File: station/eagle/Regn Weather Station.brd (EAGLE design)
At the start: 66.2 x 49 mm, 6 parts

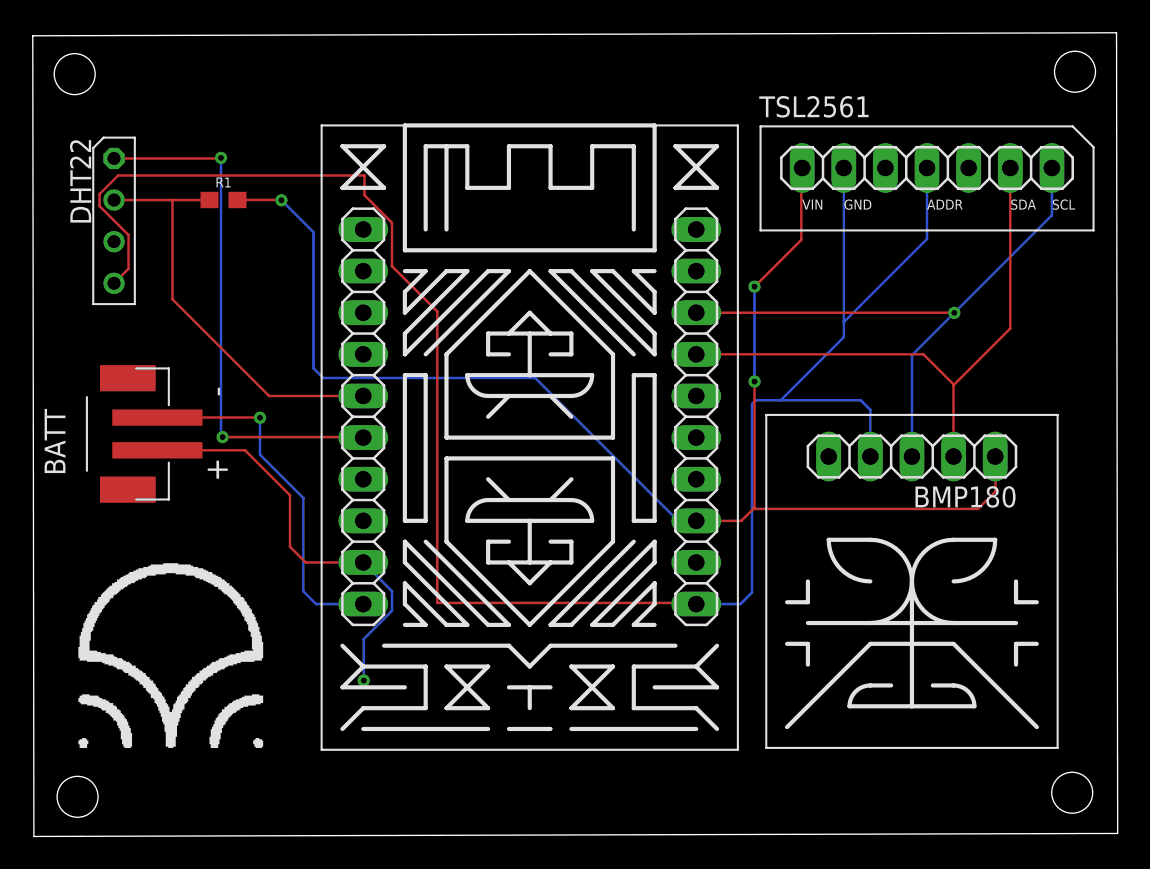
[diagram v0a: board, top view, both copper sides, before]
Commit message: Refactored PCB size and logos
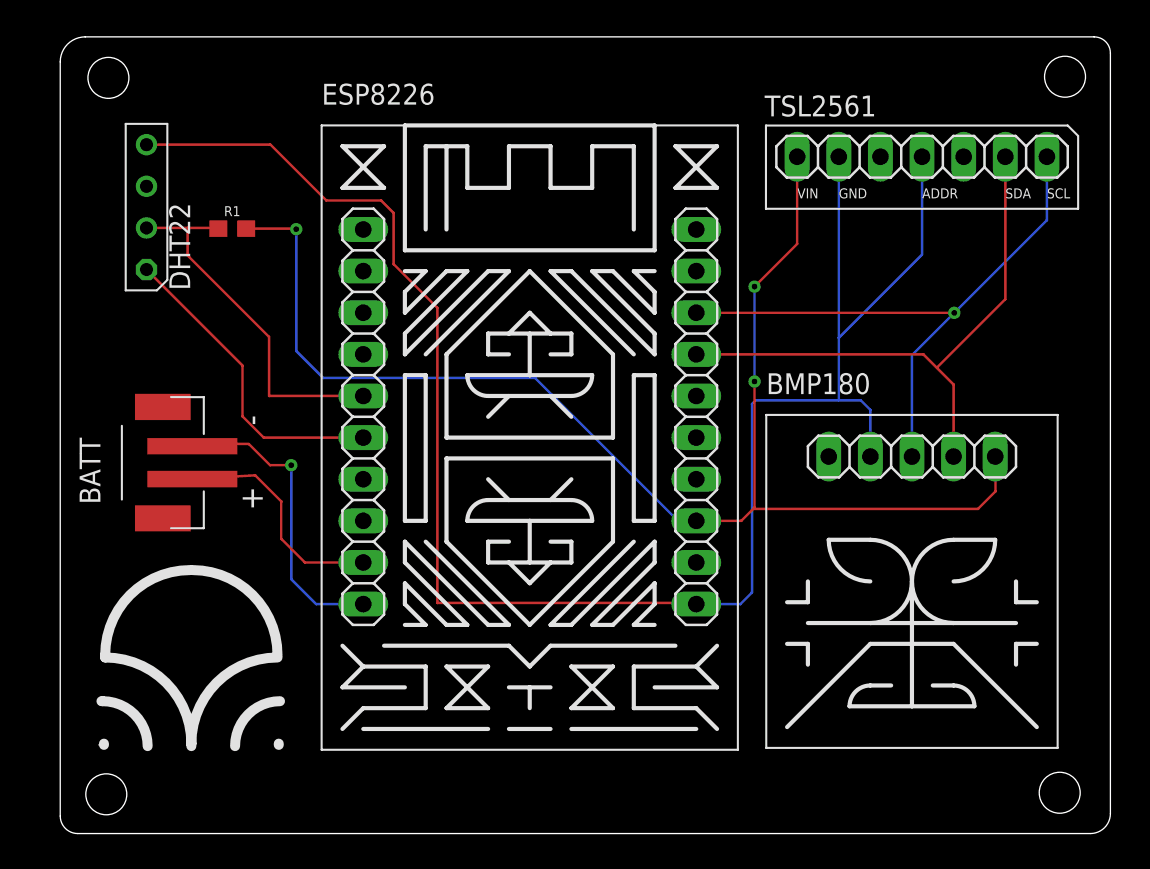
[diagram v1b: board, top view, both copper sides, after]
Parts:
- ESP8226: value ESP8266HUZZAH -> (none)
- moved BATT 2.76 mm to (7.94, 53.9)
- moved DHT22 2.15 mm to (6.94, 69.5), turned to 90 degrees
- moved R1 1.83 mm to (12.2, 68.2)
- moved TSL2561 0.75 mm to (54.3, 72.6)
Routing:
- net N$2: track 32.2 -> 19.3 mm, vias 2 -> 0
- net N$6: track 26.1 -> 14.0 mm, vias 1 -> 0
- net GND: track 120.7 -> 112.8 mm
- net N$1: track 26.0 -> 22.5 mm
- net N$7: track 21.9 -> 18.6 mm
- net 3.3V: track 84.1 -> 82.9 mm
- net N$5: track 36.9 -> 37.5 mm
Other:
- board size 66.2 x 49 mm -> 64.1 x 48.6 mm

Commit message: Increased trace width 0.6 -> 1.0 mil
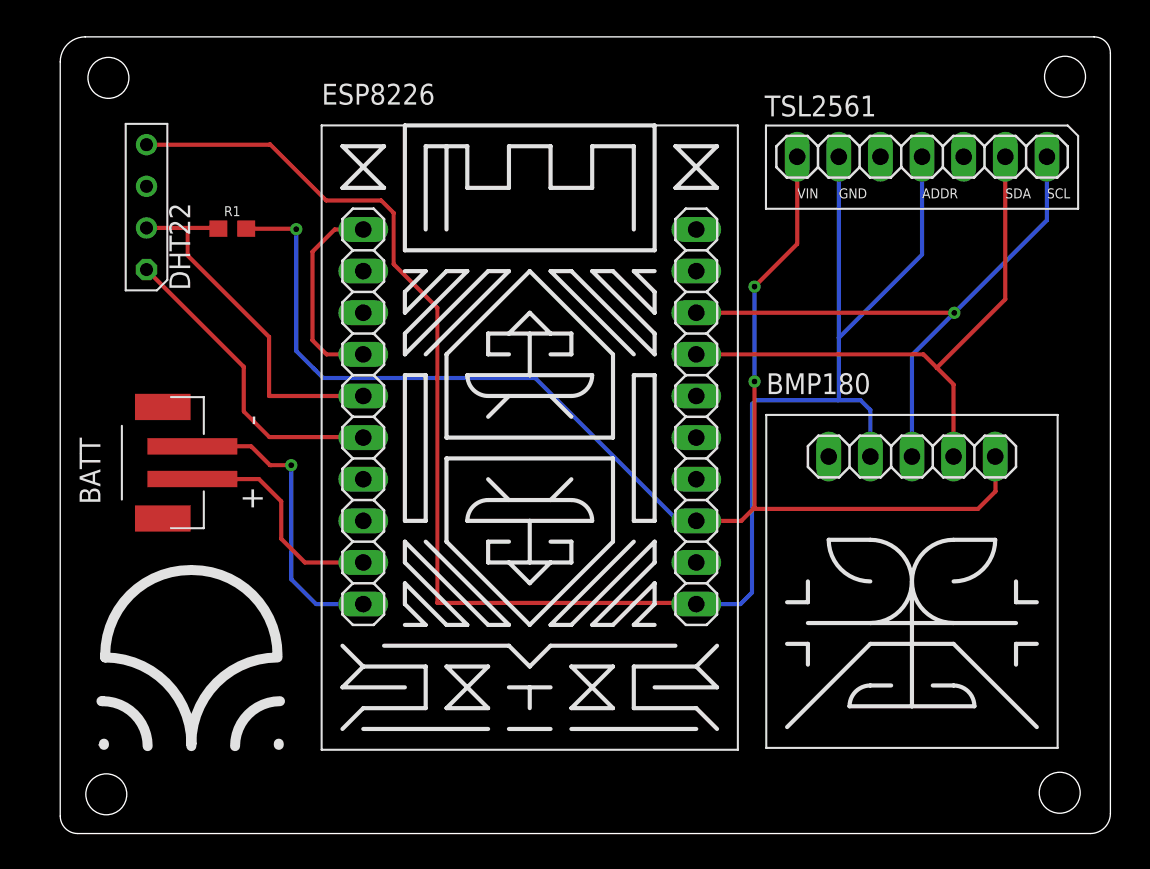
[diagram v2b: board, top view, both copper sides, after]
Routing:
- net N$4: track 0.00 -> 12.5 mm
- net GND: track 112.8 -> 111.4 mm
